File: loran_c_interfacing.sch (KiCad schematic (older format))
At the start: 18 parts, among them P401 SPI Bus A, P402 SPI Bus B, U401 74AC14, U402 74AC14

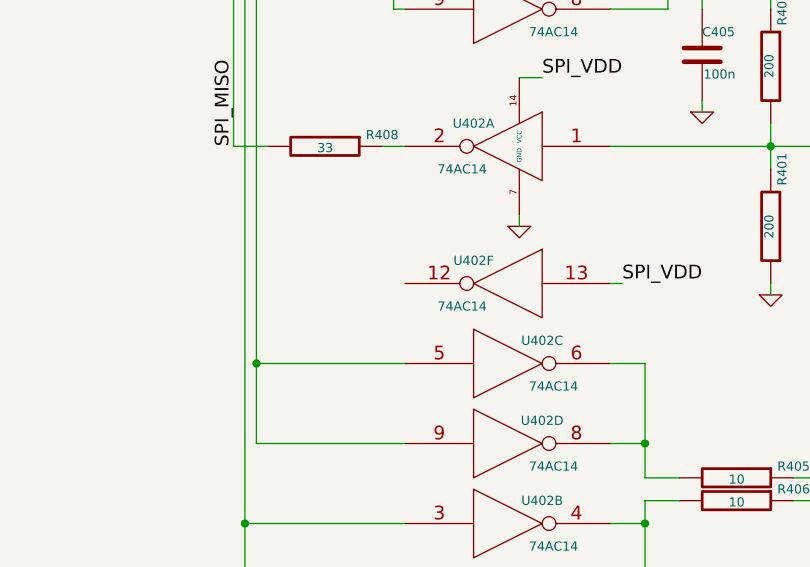
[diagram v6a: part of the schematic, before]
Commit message: Update: lots of refactoring and pin remap ..In chase for easier PCB routing PCB still not completed
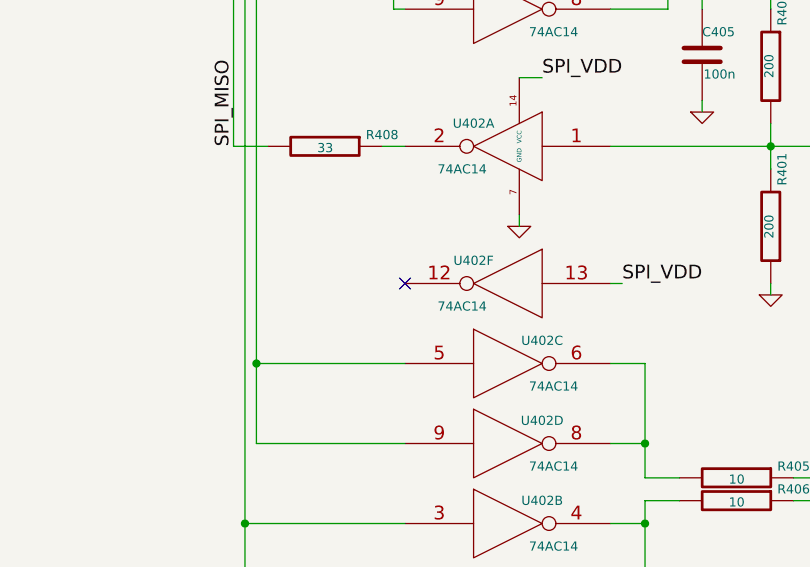
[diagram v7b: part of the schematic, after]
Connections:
- no-connect marks 2 -> 3
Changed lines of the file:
@@
 $EndComp
 $Comp
-L GND #PWR079
+L GND #PWR084
 U 1 1 52DAD917
 P 8600 2350
-F 0 "#PWR079" H 8600 2350 30  0001 C CNN
+F 0 "#PWR084" H 8600 2350 30  0001 C CNN
 F 1 "GND" H 8600 2280 30  0001 C CNN
 F 2 "" H 8600 2350 60  0000 C CNN
@@
 $EndComp
 $Comp
-L +5VD #PWR080
+L +5VD #PWR085
 U 1 1 52DAE845
 P 7650 1450
-F 0 "#PWR080" H 7650 1400 20  0001 C CNN
+F 0 "#PWR085" H 7650 1400 20  0001 C CNN
 F 1 "+5VD" H 7650 1550 30  0000 C CNN
 F 2 "" H 7650 1450 60  0000 C CNN
@@
 $EndComp
 $Comp
-L GND #PWR081
+L GND #PWR086
 U 1 1 52DAF90C
 P 8600 6100
-F 0 "#PWR081" H 8600 6100 30  0001 C CNN
+F 0 "#PWR086" H 8600 6100 30  0001 C CNN
 F 1 "GND" H 8600 6030 30  0001 C CNN
 F 2 "" H 8600 6100 60  0000 C CNN
@@
 $EndComp
 $Comp
-L +5VD #PWR082
+L +5VD #PWR087
 U 1 1 52DAF91B
 P 7650 5200
-F 0 "#PWR082" H 7650 5150 20  0001 C CNN
+F 0 "#PWR087" H 7650 5150 20  0001 C CNN
 F 1 "+5VD" H 7650 5300 30  0000 C CNN
 F 2 "" H 7650 5200 60  0000 C CNN
@@
 $EndComp
 $Comp
-L GND #PWR083
+L GND #PWR088
 U 1 1 52DD7CC9
 P 5550 2050
-F 0 "#PWR083" H 5550 2050 30  0001 C CNN
+F 0 "#PWR088" H 5550 2050 30  0001 C CNN
 F 1 "GND" H 5550 1980 30  0001 C CNN
 F 2 "" H 5550 2050 60  0000 C CNN
@@
 $EndComp
 $Comp
-L GND #PWR084
+L GND #PWR089
 U 1 1 52DD892D
 P 5650 4650
-F 0 "#PWR084" H 5650 4650 30  0001 C CNN
+F 0 "#PWR089" H 5650 4650 30  0001 C CNN
 F 1 "GND" H 5650 4580 30  0001 C CNN
 F 2 "" H 5650 4650 60  0000 C CNN
@@
 $EndComp
 $Comp
-L VDD #PWR085
+L VDD #PWR090
 U 1 1 52DDD53B
 P 3400 750
-F 0 "#PWR085" H 3400 850 30  0001 C CNN
+F 0 "#PWR090" H 3400 850 30  0001 C CNN
 F 1 "VDD" H 3400 860 30  0000 C CNN
 F 2 "" H 3400 750 60  0000 C CNN
@@
 $EndComp
 $Comp
-L GND #PWR086
+L GND #PWR091
 U 1 1 52DDD665
 P 3400 1300
-F 0 "#PWR086" H 3400 1300 30  0001 C CNN
+F 0 "#PWR091" H 3400 1300 30  0001 C CNN
 F 1 "GND" H 3400 1230 30  0001 C CNN
 F 2 "" H 3400 1300 60  0000 C CNN
@@
 $EndComp
 $Comp
-L GND #PWR087
+L GND #PWR092
 U 1 1 52DDDBEB
 P 4500 1300
-F 0 "#PWR087" H 4500 1300 30  0001 C CNN
+F 0 "#PWR092" H 4500 1300 30  0001 C CNN
 F 1 "GND" H 4500 1230 30  0001 C CNN
 F 2 "" H 4500 1300 60  0000 C CNN
@@
 $EndComp
 $Comp
-L GND #PWR088
+L GND #PWR093
 U 1 1 52DDDCDD
 P 5100 1300
-F 0 "#PWR088" H 5100 1300 30  0001 C CNN
+F 0 "#PWR093" H 5100 1300 30  0001 C CNN
 F 1 "GND" H 5100 1230 30  0001 C CNN
 F 2 "" H 5100 1300 60  0000 C CNN
@@
 $EndComp
 $Comp
-L GND #PWR089
+L GND #PWR094
 U 1 1 52DDE27D
 P 4800 1300
-F 0 "#PWR089" H 4800 1300 30  0001 C CNN
+F 0 "#PWR094" H 4800 1300 30  0001 C CNN
 F 1 "GND" H 4800 1230 30  0001 C CNN
 F 2 "" H 4800 1300 60  0000 C CNN
@@
 Connection ~ 4450 3350
 $Comp
-L PWR_FLAG #FLG090
+L PWR_FLAG #FLG095
 U 1 1 52E83610
 P 5550 750
-F 0 "#FLG090" H 5550 845 30  0001 C CNN
+F 0 "#FLG095" H 5550 845 30  0001 C CNN
 F 1 "PWR_FLAG" H 5550 930 30  0000 C CNN
 F 2 "" H 5550 750 60  0000 C CNN
@@
 	7000 5950 7700 5950
 $Comp
-L GND #PWR091
+L GND #PWR096
 U 1 1 52E6603F
 P 6750 4950
-F 0 "#PWR091" H 6750 4950 30  0001 C CNN
+F 0 "#PWR096" H 6750 4950 30  0001 C CNN
 F 1 "GND" H 6750 4880 30  0001 C CNN
 F 2 "" H 6750 4950 60  0000 C CNN
@@
 $EndComp
 $Comp
-L GND #PWR092
+L GND #PWR097
 U 1 1 52E6660B
 P 6450 4150
-F 0 "#PWR092" H 6450 4150 30  0001 C CNN
+F 0 "#PWR097" H 6450 4150 30  0001 C CNN
 F 1 "GND" H 6450 4080 30  0001 C CNN
 F 2 "" H 6450 4150 60  0000 C CNN
@@
 Wire Wire Line
 	6450 4100 6450 4150
+NoConn ~ 5150 4900
 $EndSCHEMATC
